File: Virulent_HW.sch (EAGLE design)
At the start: 98 parts, among them SW1 COM08229, SW2 COM08720, SW3 BUTTON, U1 STM32F050G6U6, U2 MAX14536

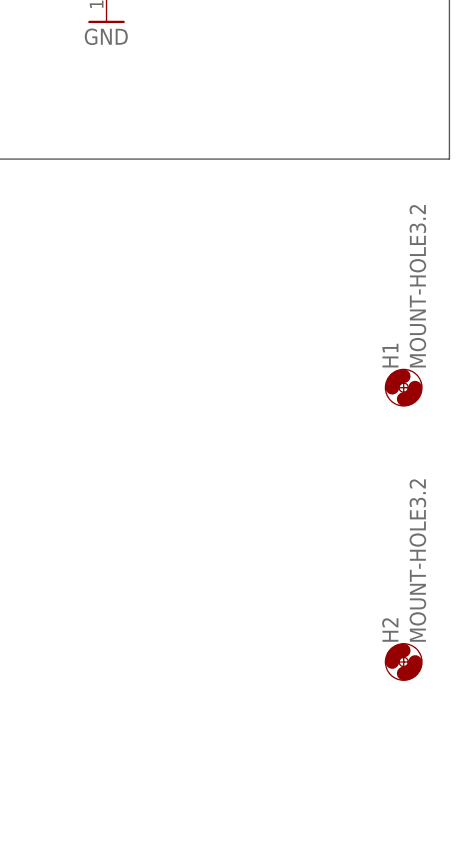
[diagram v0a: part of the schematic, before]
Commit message: Moved LDO, resized vias.
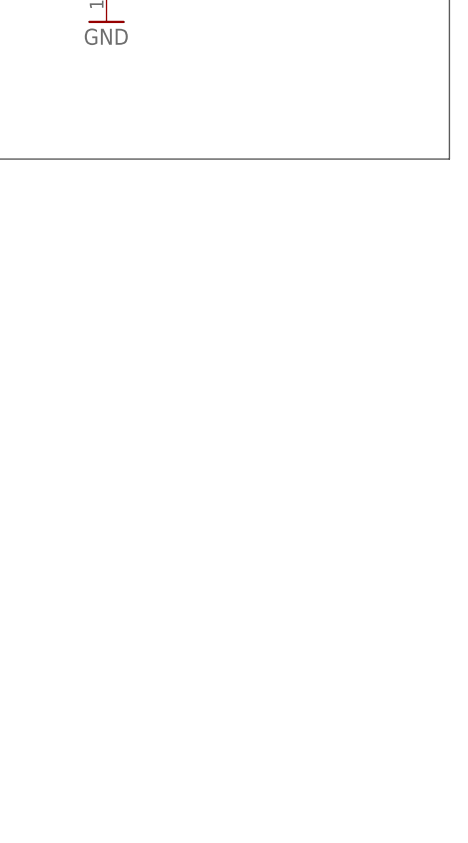
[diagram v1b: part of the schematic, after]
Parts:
- removed H1, H2: MOUNT-HOLE3.2, holes:MOUNT-HOLE3.2
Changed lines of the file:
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@@
 <part name="C35" library="rcl" deviceset="C-EU" device="C0402" value="1n"/>
 <part name="GND40" library="Virulent_HW" deviceset="GND" device=""/>
-<part name="H1" library="holes" deviceset="MOUNT-HOLE" device="3.2"/>
-<part name="H2" library="holes" deviceset="MOUNT-HOLE" device="3.2"/>
 <part name="R30" library="Virulent_HW" deviceset="R-US_" device="R0402" value="10k"/>
 <part name="P+24" library="Virulent_HW" deviceset="+3.3V" device=""/>
@@
 <instance part="C35" gate="G$1" x="43.18" y="93.98" rot="MR90"/>
 <instance part="GND40" gate="1" x="27.94" y="182.88" rot="MR0"/>
-<instance part="H1" gate="G$1" x="403.86" y="81.28" rot="R90"/>
-<instance part="H2" gate="G$1" x="403.86" y="50.8" rot="R90"/>
 <instance part="R30" gate="G$1" x="370.84" y="142.24" rot="R90"/>
 <instance part="P+24" gate="G$1" x="370.84" y="149.86"/>

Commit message: L1 needs to be remade, need SMA conn added to pin 4/pin9 of U2.
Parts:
- removed TPGND, TP_9V, TP_GND: TPTP06SQ, testpad:TPTP06SQ
- added C36, C37, C38: 0.1u, rcl:C-EUC0603
- added L1: 100u, Virulent_HW:L1008
- added TP_PB0, TP_PB1, TP_PB3, TP_PB4: TPTP06SQ, testpad:TPTP06SQ
- C20, C21, C27: value 1n -> 0.1u
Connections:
- removed net N$19: HEX1.4Y@8, R4.1, R5.2
- new net N$38: C37.1
- new net N$39: C38.1
- new net N$41: TP_PB4.TP, U1-IO.PB4@25
- new net PB0: TP_PB0.TP, U1-IO.PB0@14
- new net PB1: TP_PB1.TP, U1-IO.PB1@15
- new net PB3: TP_PB3.TP, U1-IO.PB3@24
- new net RX_OUT_L: L1.1, T1.E, T2.E
- net +9-36V: no longer TP_9V.TP
- net GND: now also C36.2, C37.2, C38.2; no longer TPGND.TP, TP_GND.TP
- net N$24: now also HEX1.4Y@8, R4.1, R5.2
- net N$6: now also C36.1
- net RX_OUT: now also L1.2; no longer T1.E, T2.E
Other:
- moved on the sheet: C25, C28, C29, C31, C35, C6, C8, CT1, NFC1, R26, R27, R28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

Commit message: fixed L1008 part. rearranged board. added SMA connector.
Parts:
- removed R15, R17: 10k, Virulent_HW:R-US_R0402
- added X1: SMA-142-0711-821/826, con-coax:SMA-142-0711-821/826
- L1: device Virulent_HW:L1008 -> rcl:L-USL1008
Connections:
- removed net N$38: C37.1
- removed net N$39: C38.1
- net GND: no longer R15.1, R17.1
- net N$20: now also X1.1
- net N$32: now also X1.2
- net N$34: no longer R17.2
- net NRESET_SOFT: now also C37.1
- net TEAMID1: no longer R15.2
- net TRIGGER: now also C38.1
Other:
- moved on the sheet: C25, C29, CT1, NFC1, R14, R16, R29

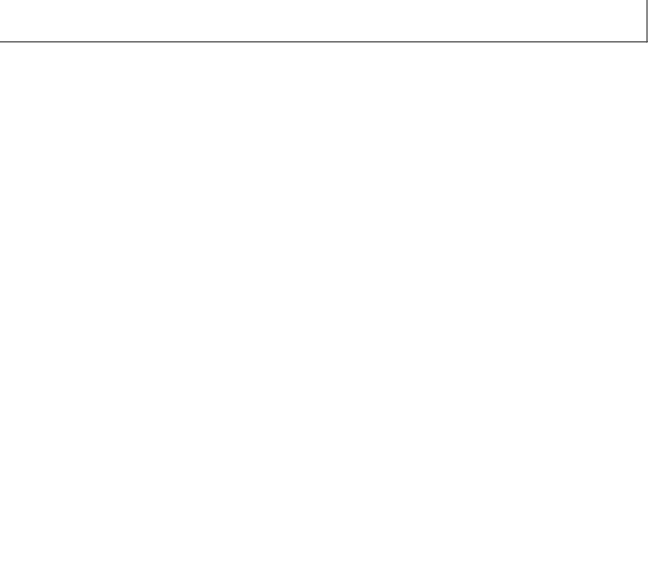
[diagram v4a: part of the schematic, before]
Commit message: Added mount holes, completed layout.
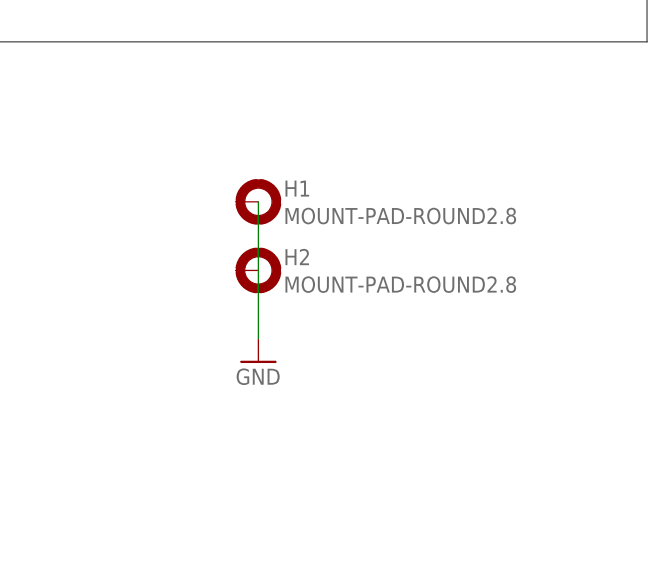
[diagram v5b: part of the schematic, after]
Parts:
- added H1, H2: MOUNT-PAD-ROUND2.8, holes:MOUNT-PAD-ROUND2.8
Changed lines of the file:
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@@
 <part name="L1" library="rcl" deviceset="L-US" device="L1008" value="100u"/>
 <part name="X1" library="con-coax" deviceset="SMA-" device="142-0711-821/826"/>
+<part name="H1" library="holes" deviceset="MOUNT-PAD-ROUND" device="2.8"/>
+<part name="H2" library="holes" deviceset="MOUNT-PAD-ROUND" device="2.8"/>
+<part name="GND16" library="Virulent_HW" deviceset="GND" device=""/>
 </parts>
 <sheets>
@@
 <instance part="L1" gate="G$1" x="147.32" y="93.98" rot="R90"/>
 <instance part="X1" gate="G1" x="33.02" y="114.3" rot="R90"/>
+<instance part="H1" gate="G$1" x="365.76" y="88.9"/>
+<instance part="H2" gate="G$1" x="365.76" y="81.28"/>
+<instance part="GND16" gate="1" x="365.76" y="71.12"/>
 </instances>
 <busses>
@@
 <junction x="12.7" y="48.26"/>
 </segment>
+<segment>
+<wire x1="365.76" y1="88.9" x2="365.76" y2="73.66" width="0.1524" layer="91"/>
+<pinref part="GND16" gate="1" pin="GND"/>
+</segment>
 </net>

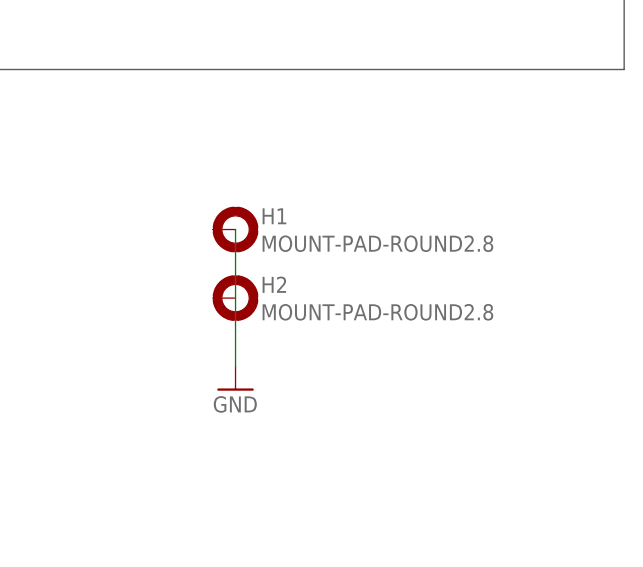
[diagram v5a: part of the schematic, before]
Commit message: Connected mounting holes to GND.
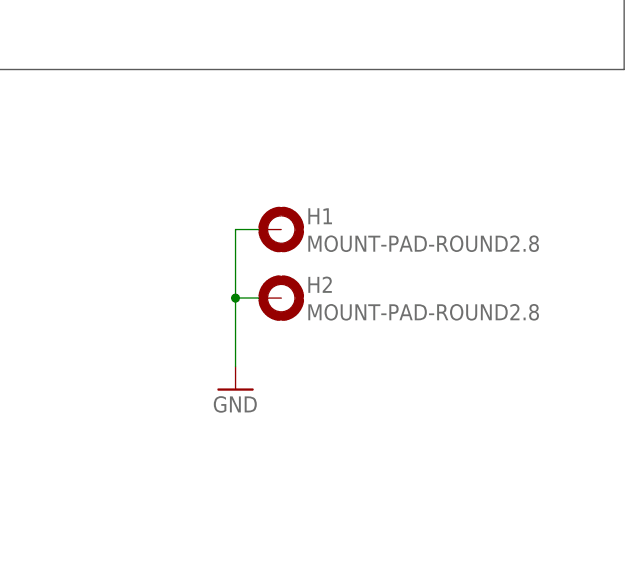
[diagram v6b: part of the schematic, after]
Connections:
- net GND: now also H1.MOUNT, H2.MOUNT
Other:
- moved on the sheet: H1, H2
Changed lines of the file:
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@@
 <instance part="L1" gate="G$1" x="147.32" y="93.98" rot="R90"/>
 <instance part="X1" gate="G1" x="33.02" y="114.3" rot="R90"/>
-<instance part="H1" gate="G$1" x="365.76" y="88.9"/>
-<instance part="H2" gate="G$1" x="365.76" y="81.28"/>
+<instance part="H1" gate="G$1" x="370.84" y="88.9"/>
+<instance part="H2" gate="G$1" x="370.84" y="81.28"/>
 <instance part="GND16" gate="1" x="365.76" y="71.12"/>
 </instances>
@@
 </segment>
 <segment>
-<wire x1="365.76" y1="88.9" x2="365.76" y2="73.66" width="0.1524" layer="91"/>
+<wire x1="365.76" y1="88.9" x2="365.76" y2="81.28" width="0.1524" layer="91"/>
 <pinref part="GND16" gate="1" pin="GND"/>
+<pinref part="H1" gate="G$1" pin="MOUNT"/>
+<wire x1="365.76" y1="81.28" x2="365.76" y2="73.66" width="0.1524" layer="91"/>
+<wire x1="365.76" y1="88.9" x2="368.3" y2="88.9" width="0.1524" layer="91"/>
+<pinref part="H2" gate="G$1" pin="MOUNT"/>
+<wire x1="365.76" y1="81.28" x2="368.3" y2="81.28" width="0.1524" layer="91"/>
+<junction x="365.76" y="81.28"/>
 </segment>
 </net>
